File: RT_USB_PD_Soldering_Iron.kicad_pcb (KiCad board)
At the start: 4 copper layers, 75 x 11 mm, 60 parts, among them J1 USB4105-GF-A, J2 35RASMT4BHNTRX, J3 Conn_02x03_Odd_Even, SW1 SW_Push, SW2 SW_Push, U1 SPX3819M5-L-3-3, U2 BMI270, U3 DRTR5V0U4S-7, U5 STM32G431Kxxx, U6 TPS25982ONRGET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

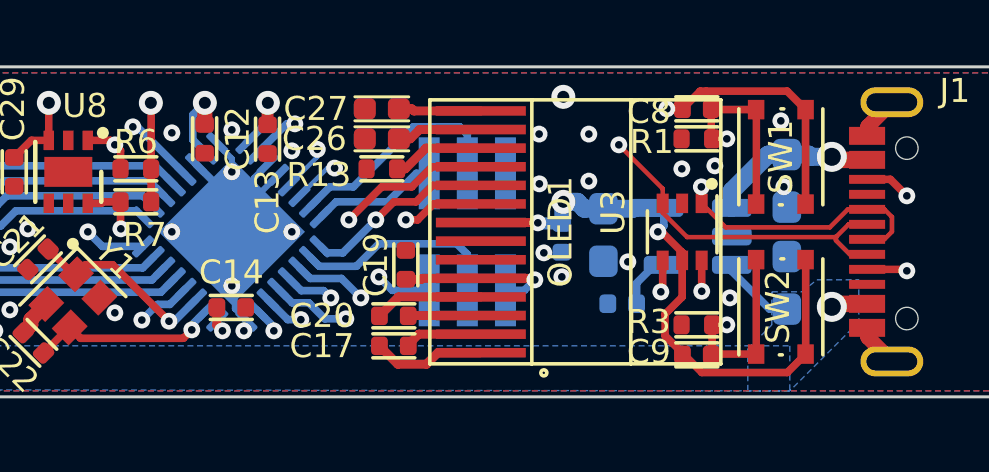
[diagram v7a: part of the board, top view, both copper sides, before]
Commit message: Modify CC lines
Add capacitors to CC lines. Tie in DBCC to the CC lines.
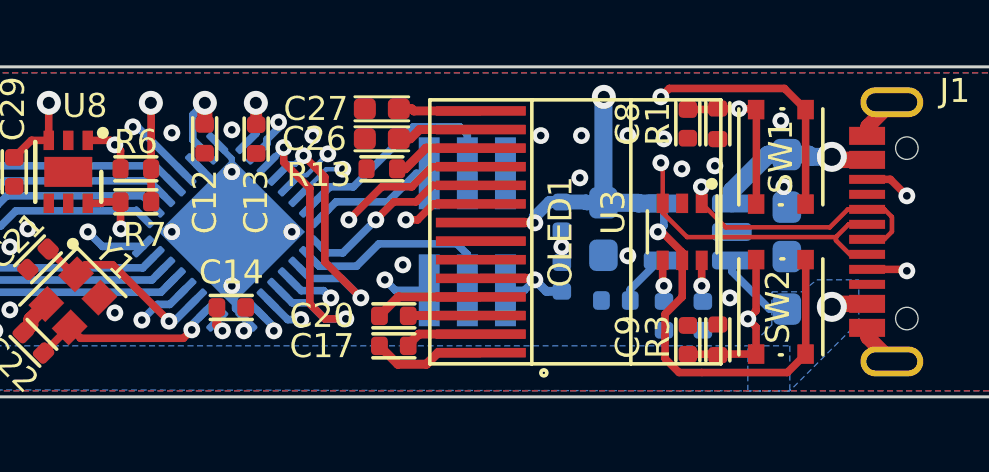
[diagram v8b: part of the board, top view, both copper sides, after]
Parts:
- added C6: 220pF 50v, local:C_0402_1005Metric, B.Cu at (162.9, 127.8)
- added C7: 220pF 50v, local:C_0402_1005Metric, B.Cu at (161.6, 127.8)
- C19: moved to B.Cu
- moved C19 5.22 mm to (158.2, 126.5)
- moved R1 0.86 mm to (163.4, 121.4), turned to -90 degrees
- moved R3 0.86 mm to (163.4, 128.6), turned to 90 degrees
- moved C18 0.71 mm to (158.2, 124.5)
- moved C8 0.58 mm to (162.4, 121.4), turned to 90 degrees
- moved C9 0.58 mm to (162.4, 128.6), turned to -90 degrees
- moved C13 0.38 mm to (148.0, 121.9)
- moved C3 0.24 mm to (160.0, 127.3)
- moved C2 0.20 mm to (159.6, 124.9)
- moved U1 0.15 mm to (162.7, 125.0)
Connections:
- C8 pad 1: +3V3 -> GND
- C9 pad 1: +3V3 -> GND
- U5 pad 19: GND -> /CC1
- U5 pad 20: GND -> /CC2
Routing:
- net /CC1: track 24.4 -> 32.5 mm, vias 3 -> 4
- net /CC2: track 24.7 -> 31.6 mm, vias 3 -> 4
- net GND: track 21.0 -> 17.2 mm, vias 61 -> 62
- net +3V3: track 99.1 -> 97.0 mm, vias 12 -> 11
